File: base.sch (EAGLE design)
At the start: 6 parts

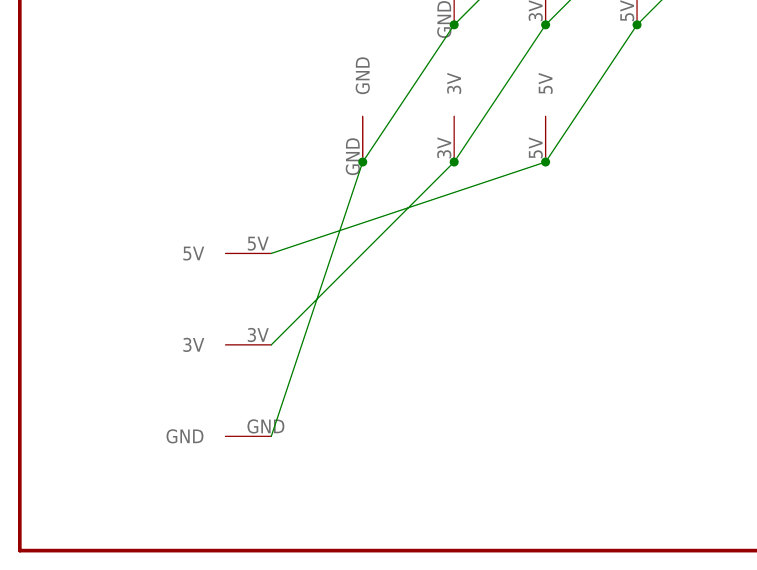
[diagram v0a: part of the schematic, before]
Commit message: linked missing powerpole set, corrected physical mount footprint
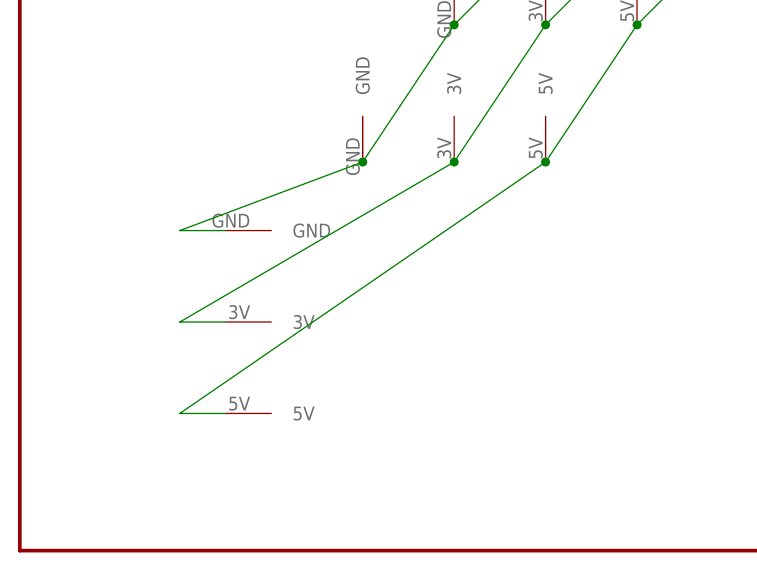
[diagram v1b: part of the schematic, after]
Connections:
- net N$1 renamed GND
- net N$3 renamed 5V
- net N$4 renamed 3V
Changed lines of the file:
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@@
 <instance part="FRAME1" gate="G$1" x="0" y="0"/>
 <instance part="FRAME1" gate="G$2" x="165.1" y="0"/>
-<instance part="U$1" gate="G$1" x="27.94" y="22.86" rot="R90"/>
+<instance part="U$1" gate="G$1" x="22.86" y="25.4" rot="R270"/>
 <instance part="U$2" gate="G$1" x="48.26" y="43.18"/>
 <instance part="U$3" gate="G$1" x="73.66" y="73.66"/>
@@
 </busses>
 <nets>
-<net name="N$1" class="0">
+<net name="GND" class="0">
 <segment>
-<pinref part="U$1" gate="G$1" pin="GND"/>
 <pinref part="U$2" gate="G$1" pin="GND"/>
-<wire x1="27.94" y1="12.7" x2="38.1" y2="43.18" width="0.1524" layer="91"/>
 <pinref part="U$5" gate="G$1" pin="GND"/>
 <wire x1="38.1" y1="43.18" x2="48.26" y2="58.42" width="0.1524" layer="91"/>
-<junction x="38.1" y="43.18"/>
 <pinref part="U$3" gate="G$1" pin="GND"/>
 <wire x1="48.26" y1="58.42" x2="63.5" y2="73.66" width="0.1524" layer="91"/>
@@
 <wire x1="83.82" y1="101.6" x2="73.66" y2="88.9" width="0.1524" layer="91"/>
 <junction x="73.66" y="88.9"/>
+<wire x1="38.1" y1="43.18" x2="17.78" y2="35.56" width="0.1524" layer="91"/>
+<junction x="38.1" y="43.18"/>
+<pinref part="U$1" gate="G$1" pin="GND"/>
+<wire x1="22.86" y1="35.56" x2="17.78" y2="35.56" width="0.1524" layer="91"/>
 </segment>
 </net>
-<net name="N$3" class="0">
+<net name="5V" class="0">
 <segment>
-<pinref part="U$1" gate="G$1" pin="5V"/>
 <pinref part="U$2" gate="G$1" pin="5V"/>
-<wire x1="27.94" y1="33.02" x2="58.42" y2="43.18" width="0.1524" layer="91"/>
 <pinref part="U$5" gate="G$1" pin="5V"/>
 <wire x1="58.42" y1="43.18" x2="68.58" y2="58.42" width="0.1524" layer="91"/>
-<junction x="58.42" y="43.18"/>
 <pinref part="U$3" gate="G$1" pin="5V"/>
 <wire x1="68.58" y1="58.42" x2="83.82" y2="73.66" width="0.1524" layer="91"/>
@@
 <wire x1="93.98" y1="88.9" x2="104.14" y2="101.6" width="0.1524" layer="91"/>
 <junction x="93.98" y="88.9"/>
+<wire x1="58.42" y1="43.18" x2="17.78" y2="15.24" width="0.1524" layer="91"/>
+<junction x="58.42" y="43.18"/>
+<pinref part="U$1" gate="G$1" pin="5V"/>
+<wire x1="17.78" y1="15.24" x2="22.86" y2="15.24" width="0.1524" layer="91"/>
 </segment>
 </net>
-<net name="N$4" class="0">
+<net name="3V" class="0">
 <segment>
 <pinref part="U$6" gate="G$1" pin="3V"/>
@@
 <wire x1="73.66" y1="73.66" x2="58.42" y2="58.42" width="0.1524" layer="91"/>
 <junction x="73.66" y="73.66"/>
-<pinref part="U$1" gate="G$1" pin="3V"/>
 <pinref part="U$2" gate="G$1" pin="3V"/>
-<wire x1="27.94" y1="22.86" x2="48.26" y2="43.18" width="0.1524" layer="91"/>
 <wire x1="58.42" y1="58.42" x2="48.26" y2="43.18" width="0.1524" layer="91"/>
 <junction x="58.42" y="58.42"/>
+<wire x1="48.26" y1="43.18" x2="17.78" y2="25.4" width="0.1524" layer="91"/>
 <junction x="48.26" y="43.18"/>
+<pinref part="U$1" gate="G$1" pin="3V"/>
+<wire x1="22.86" y1="25.4" x2="17.78" y2="25.4" width="0.1524" layer="91"/>
 </segment>
 </net>

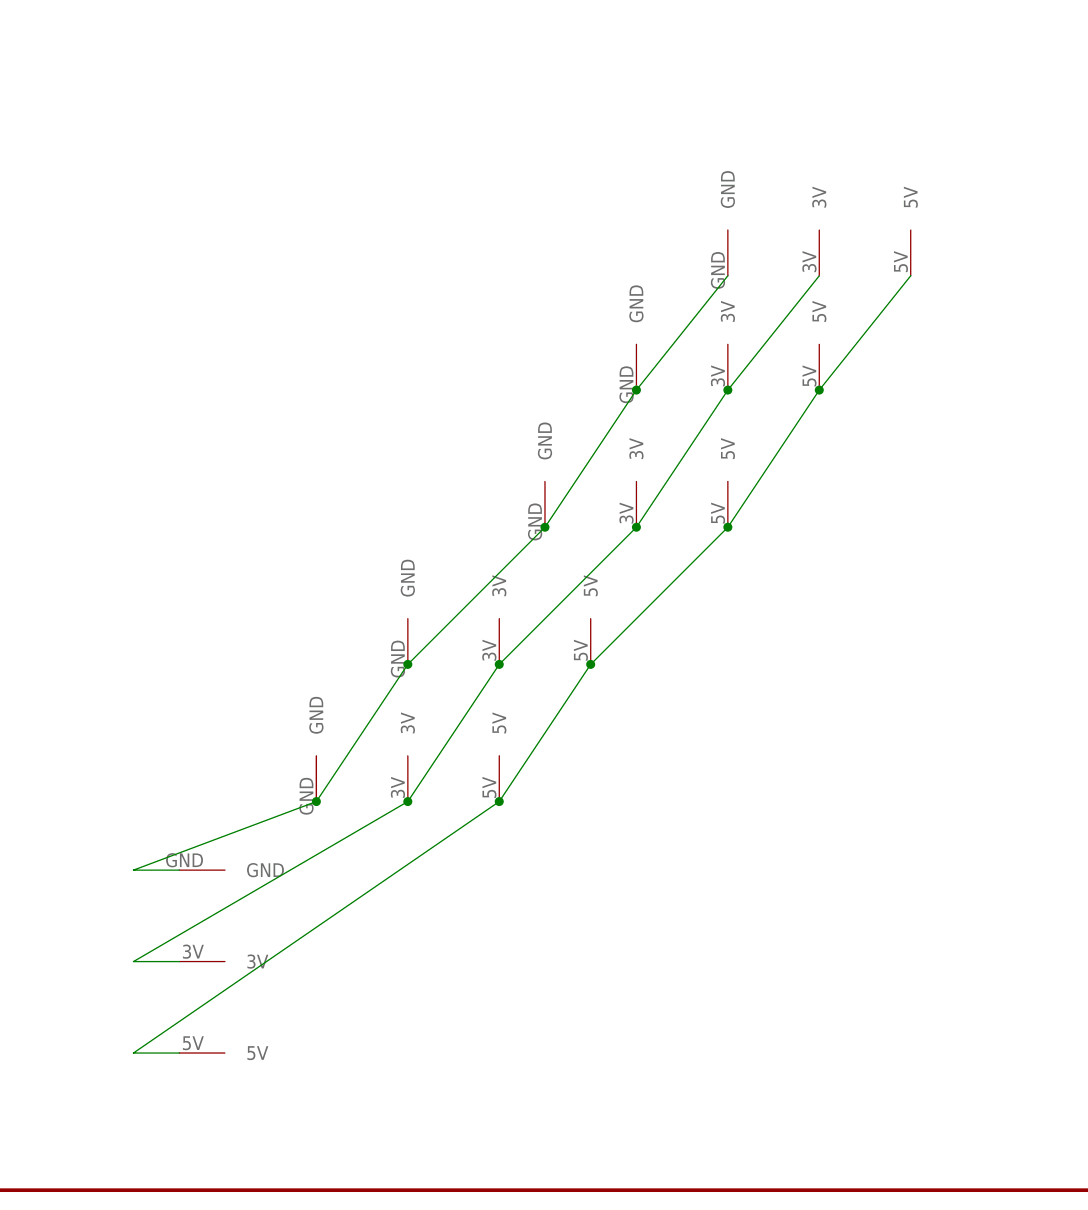
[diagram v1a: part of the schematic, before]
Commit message: split traces between top and bottom copper to reduce trace width
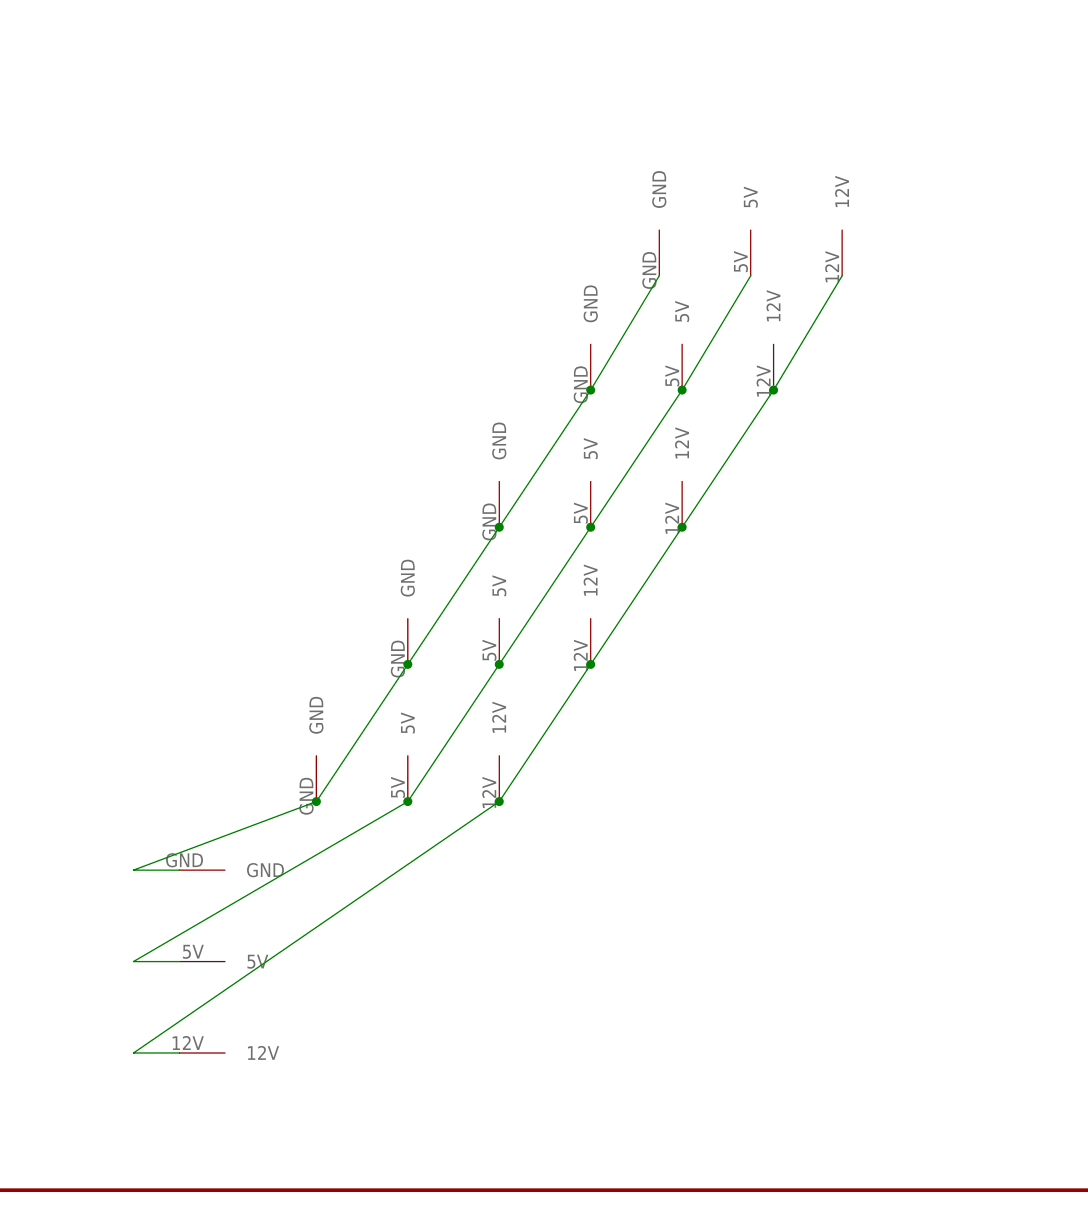
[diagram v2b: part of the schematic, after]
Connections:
- removed net 3V: U$1.3V, U$2.3V, U$3.3V, U$4.3V, U$5.3V, U$6.3V
- new net 12V: U$1.12V, U$2.12V, U$3.12V, U$4.12V, U$5.12V, U$6.12V
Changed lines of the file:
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@@
 <class number="0" name="default" width="0" drill="0">
+</class>
+<class number="1" name="Vcc" width="3.6068" drill="0.381">
+<clearance class="1" value="0.254"/>
 </class>
 </classes>
@@
 <instance part="U$1" gate="G$1" x="22.86" y="25.4" rot="R270"/>
 <instance part="U$2" gate="G$1" x="48.26" y="43.18"/>
-<instance part="U$3" gate="G$1" x="73.66" y="73.66"/>
-<instance part="U$4" gate="G$1" x="83.82" y="88.9"/>
+<instance part="U$3" gate="G$1" x="68.58" y="73.66"/>
+<instance part="U$4" gate="G$1" x="78.74" y="88.9"/>
 <instance part="U$5" gate="G$1" x="58.42" y="58.42"/>
-<instance part="U$6" gate="G$1" x="93.98" y="101.6"/>
+<instance part="U$6" gate="G$1" x="86.36" y="101.6"/>
 </instances>
 <busses>
@@
 <wire x1="38.1" y1="43.18" x2="48.26" y2="58.42" width="0.1524" layer="91"/>
 <pinref part="U$3" gate="G$1" pin="GND"/>
-<wire x1="48.26" y1="58.42" x2="63.5" y2="73.66" width="0.1524" layer="91"/>
+<wire x1="48.26" y1="58.42" x2="58.42" y2="73.66" width="0.1524" layer="91"/>
 <junction x="48.26" y="58.42"/>
 <pinref part="U$4" gate="G$1" pin="GND"/>
-<wire x1="63.5" y1="73.66" x2="73.66" y2="88.9" width="0.1524" layer="91"/>
-<junction x="63.5" y="73.66"/>
+<wire x1="58.42" y1="73.66" x2="68.58" y2="88.9" width="0.1524" layer="91"/>
+<junction x="58.42" y="73.66"/>
 <pinref part="U$6" gate="G$1" pin="GND"/>
-<wire x1="83.82" y1="101.6" x2="73.66" y2="88.9" width="0.1524" layer="91"/>
-<junction x="73.66" y="88.9"/>
+<wire x1="76.2" y1="101.6" x2="68.58" y2="88.9" width="0.1524" layer="91"/>
+<junction x="68.58" y="88.9"/>
 <wire x1="38.1" y1="43.18" x2="17.78" y2="35.56" width="0.1524" layer="91"/>
 <junction x="38.1" y="43.18"/>
@@
 </segment>
 </net>
+<net name="12V" class="0">
+<segment>
+<pinref part="U$2" gate="G$1" pin="12V"/>
+<pinref part="U$5" gate="G$1" pin="12V"/>
+<wire x1="58.42" y1="43.18" x2="68.58" y2="58.42" width="0.1524" layer="91"/>
+<wire x1="58.42" y1="43.18" x2="17.78" y2="15.24" width="0.1524" layer="91"/>
+<junction x="58.42" y="43.18"/>
+<pinref part="U$1" gate="G$1" pin="12V"/>
+<wire x1="17.78" y1="15.24" x2="22.86" y2="15.24" width="0.1524" layer="91"/>
+<pinref part="U$3" gate="G$1" pin="12V"/>
+<wire x1="68.58" y1="58.42" x2="78.74" y2="73.66" width="0.1524" layer="91"/>
+<junction x="68.58" y="58.42"/>
+<pinref part="U$6" gate="G$1" pin="12V"/>
+<pinref part="U$4" gate="G$1" pin="12V"/>
+<wire x1="88.9" y1="88.9" x2="96.52" y2="101.6" width="0.1524" layer="91"/>
+<wire x1="78.74" y1="73.66" x2="88.9" y2="88.9" width="0.1524" layer="91"/>
+<junction x="78.74" y="73.66"/>
+<junction x="88.9" y="88.9"/>
+</segment>
+</net>
 <net name="5V" class="0">
 <segment>
+<pinref part="U$6" gate="G$1" pin="5V"/>
+<pinref part="U$4" gate="G$1" pin="5V"/>
+<wire x1="86.36" y1="101.6" x2="78.74" y2="88.9" width="0.1524" layer="91"/>
+<pinref part="U$3" gate="G$1" pin="5V"/>
+<wire x1="78.74" y1="88.9" x2="68.58" y2="73.66" width="0.1524" layer="91"/>
+<junction x="78.74" y="88.9"/>
+<pinref part="U$5" gate="G$1" pin="5V"/>
+<wire x1="68.58" y1="73.66" x2="58.42" y2="58.42" width="0.1524" layer="91"/>
+<junction x="68.58" y="73.66"/>
 <pinref part="U$2" gate="G$1" pin="5V"/>
-<pinref part="U$5" gate="G$1" pin="5V"/>
-<wire x1="58.42" y1="43.18" x2="68.58" y2="58.42" width="0.1524" layer="91"/>
-<pinref part="U$3" gate="G$1" pin="5V"/>
-<wire x1="68.58" y1="58.42" x2="83.82" y2="73.66" width="0.1524" layer="91"/>
-<junction x="68.58" y="58.42"/>
-<pinref part="U$4" gate="G$1" pin="5V"/>
-<wire x1="83.82" y1="73.66" x2="93.98" y2="88.9" width="0.1524" layer="91"/>
-<junction x="83.82" y="73.66"/>
-<pinref part="U$6" gate="G$1" pin="5V"/>
-<wire x1="93.98" y1="88.9" x2="104.14" y2="101.6" width="0.1524" layer="91"/>
-<junction x="93.98" y="88.9"/>
-<wire x1="58.42" y1="43.18" x2="17.78" y2="15.24" width="0.1524" layer="91"/>
-<junction x="58.42" y="43.18"/>
-<pinref part="U$1" gate="G$1" pin="5V"/>
-<wire x1="17.78" y1="15.24" x2="22.86" y2="15.24" width="0.1524" layer="91"/>
-</segment>
-</net>
-<net name="3V" class="0">
-<segment>
-<pinref part="U$6" gate="G$1" pin="3V"/>
-<pinref part="U$4" gate="G$1" pin="3V"/>
-<wire x1="93.98" y1="101.6" x2="83.82" y2="88.9" width="0.1524" layer="91"/>
-<pinref part="U$3" gate="G$1" pin="3V"/>
-<wire x1="83.82" y1="88.9" x2="73.66" y2="73.66" width="0.1524" layer="91"/>
-<junction x="83.82" y="88.9"/>
-<pinref part="U$5" gate="G$1" pin="3V"/>
-<wire x1="73.66" y1="73.66" x2="58.42" y2="58.42" width="0.1524" layer="91"/>
-<junction x="73.66" y="73.66"/>
-<pinref part="U$2" gate="G$1" pin="3V"/>
 <wire x1="58.42" y1="58.42" x2="48.26" y2="43.18" width="0.1524" layer="91"/>
 <junction x="58.42" y="58.42"/>
 <wire x1="48.26" y1="43.18" x2="17.78" y2="25.4" width="0.1524" layer="91"/>
 <junction x="48.26" y="43.18"/>
-<pinref part="U$1" gate="G$1" pin="3V"/>
+<pinref part="U$1" gate="G$1" pin="5V"/>
 <wire x1="22.86" y1="25.4" x2="17.78" y2="25.4" width="0.1524" layer="91"/>
 </segment>
